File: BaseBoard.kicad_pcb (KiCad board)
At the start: 2 copper layers, 225 x 225 mm, 170 parts, among them Q1 MMBT2222A-7-F, Q10 IRLML6401TRPBF, Q11 MMBT2222A-7-F, Q12 IRLML6401TRPBF, Q13 MMBT2222A-7-F, Q14 IRLML6401TRPBF, Q15 MMBT2222A-7-F, Q16 IRLML6401TRPBF, Q2 IRLML6401TRPBF, Q3 MMBT2222A-7-F, Q4 IRLML6401TRPBF, Q5 MMBT2222A-7-F, Q6 IRLML6401TRPBF, Q7 MMBT2222A-7-F, Q8 IRLML6401TRPBF, Q9 MMBT2222A-7-F, U1 TLC5971PWPR, U10 TLC5971PWPR, U11 TLC5971PWPR, U12 TLC5971PWPR, U13 TLC5971PWPR, U14 TLC5971PWPR, U15 TLC5971PWPR, U16 TLC5971PWPR, U2 TLC5971PWPR, U3 TLC5971PWPR, U4 TLC5971PWPR, U5 TLC5971PWPR, U6 TLC5971PWPR, U7 TLC5971PWPR, U8 TLC5971PWPR, U9 TLC5971PWPR

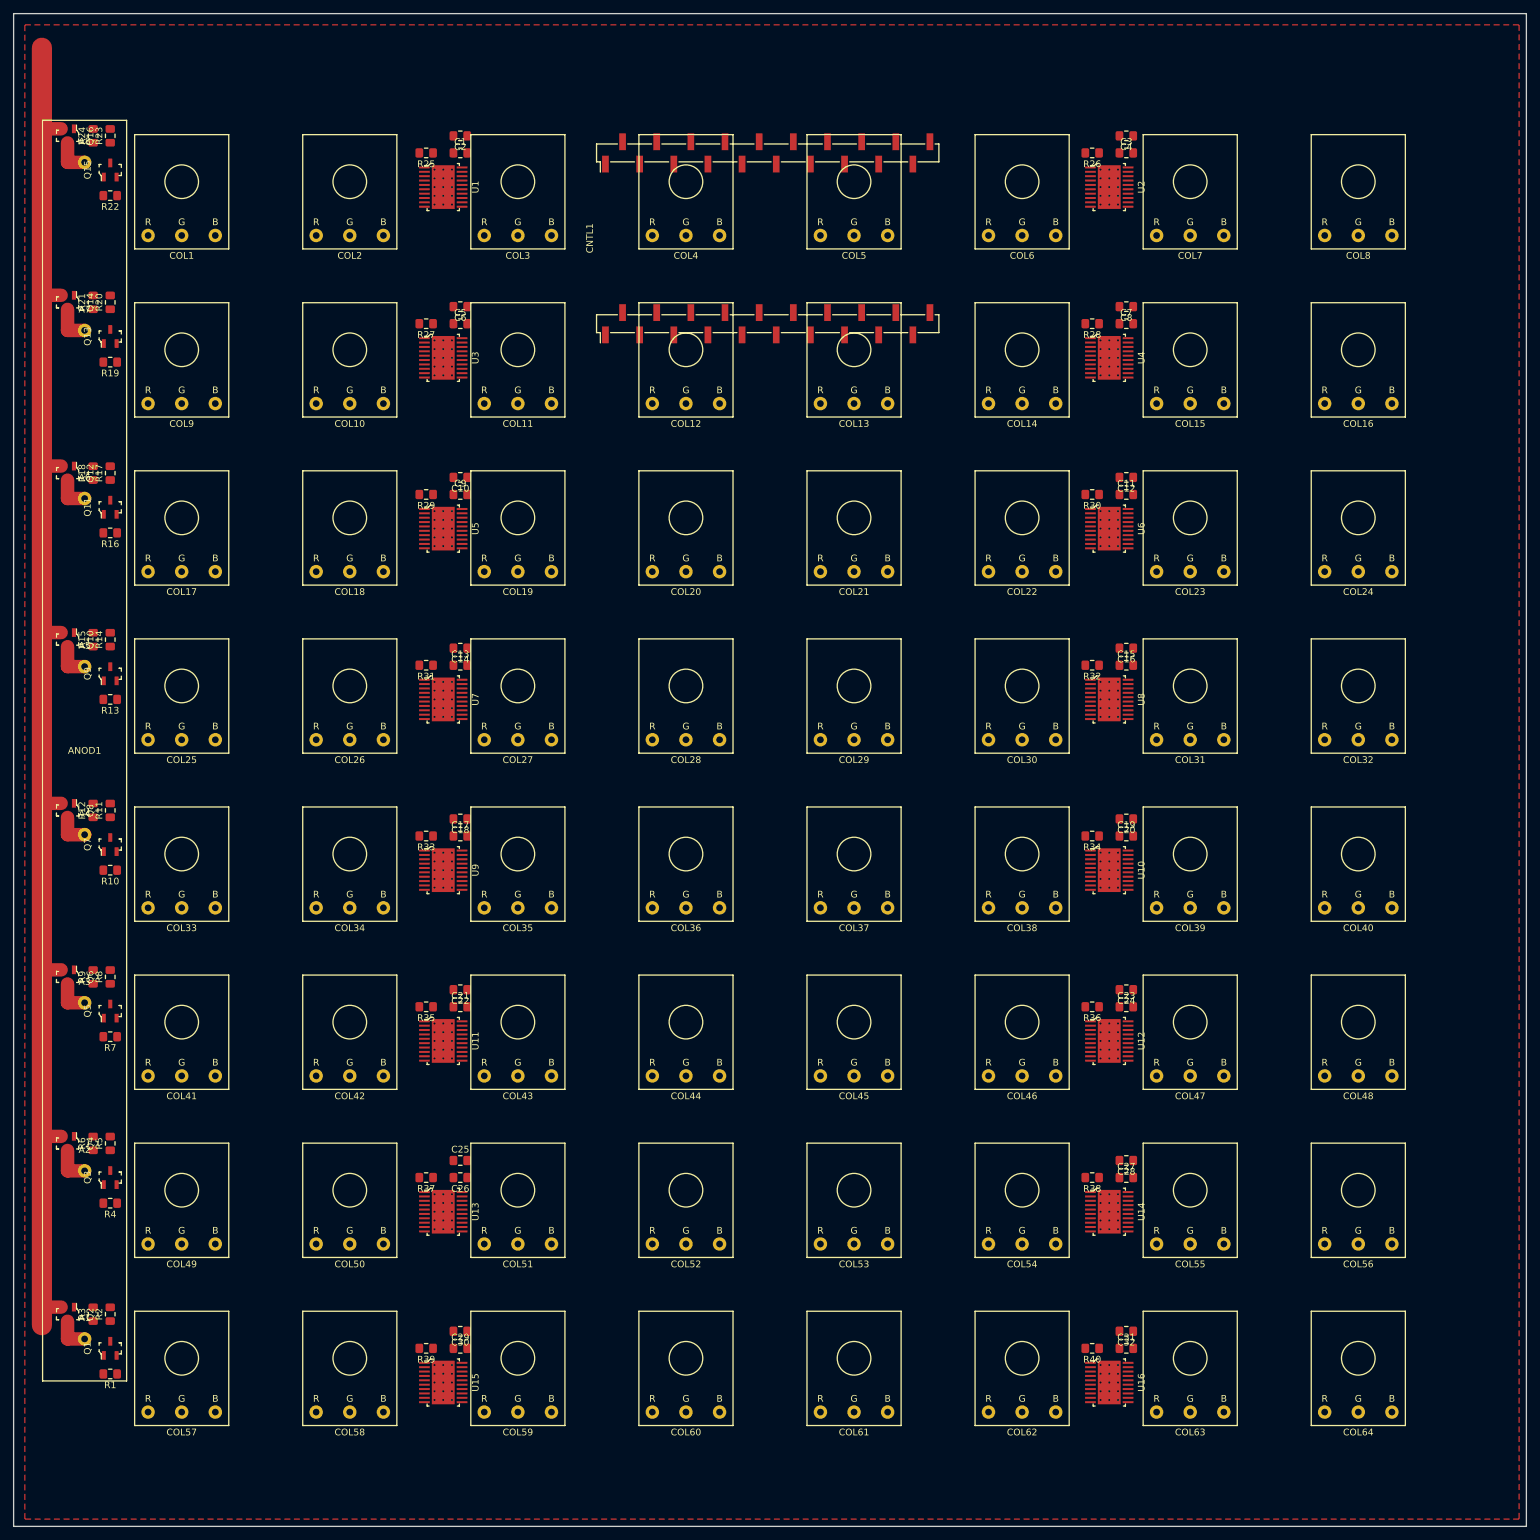
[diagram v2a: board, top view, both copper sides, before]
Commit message: Update footprints
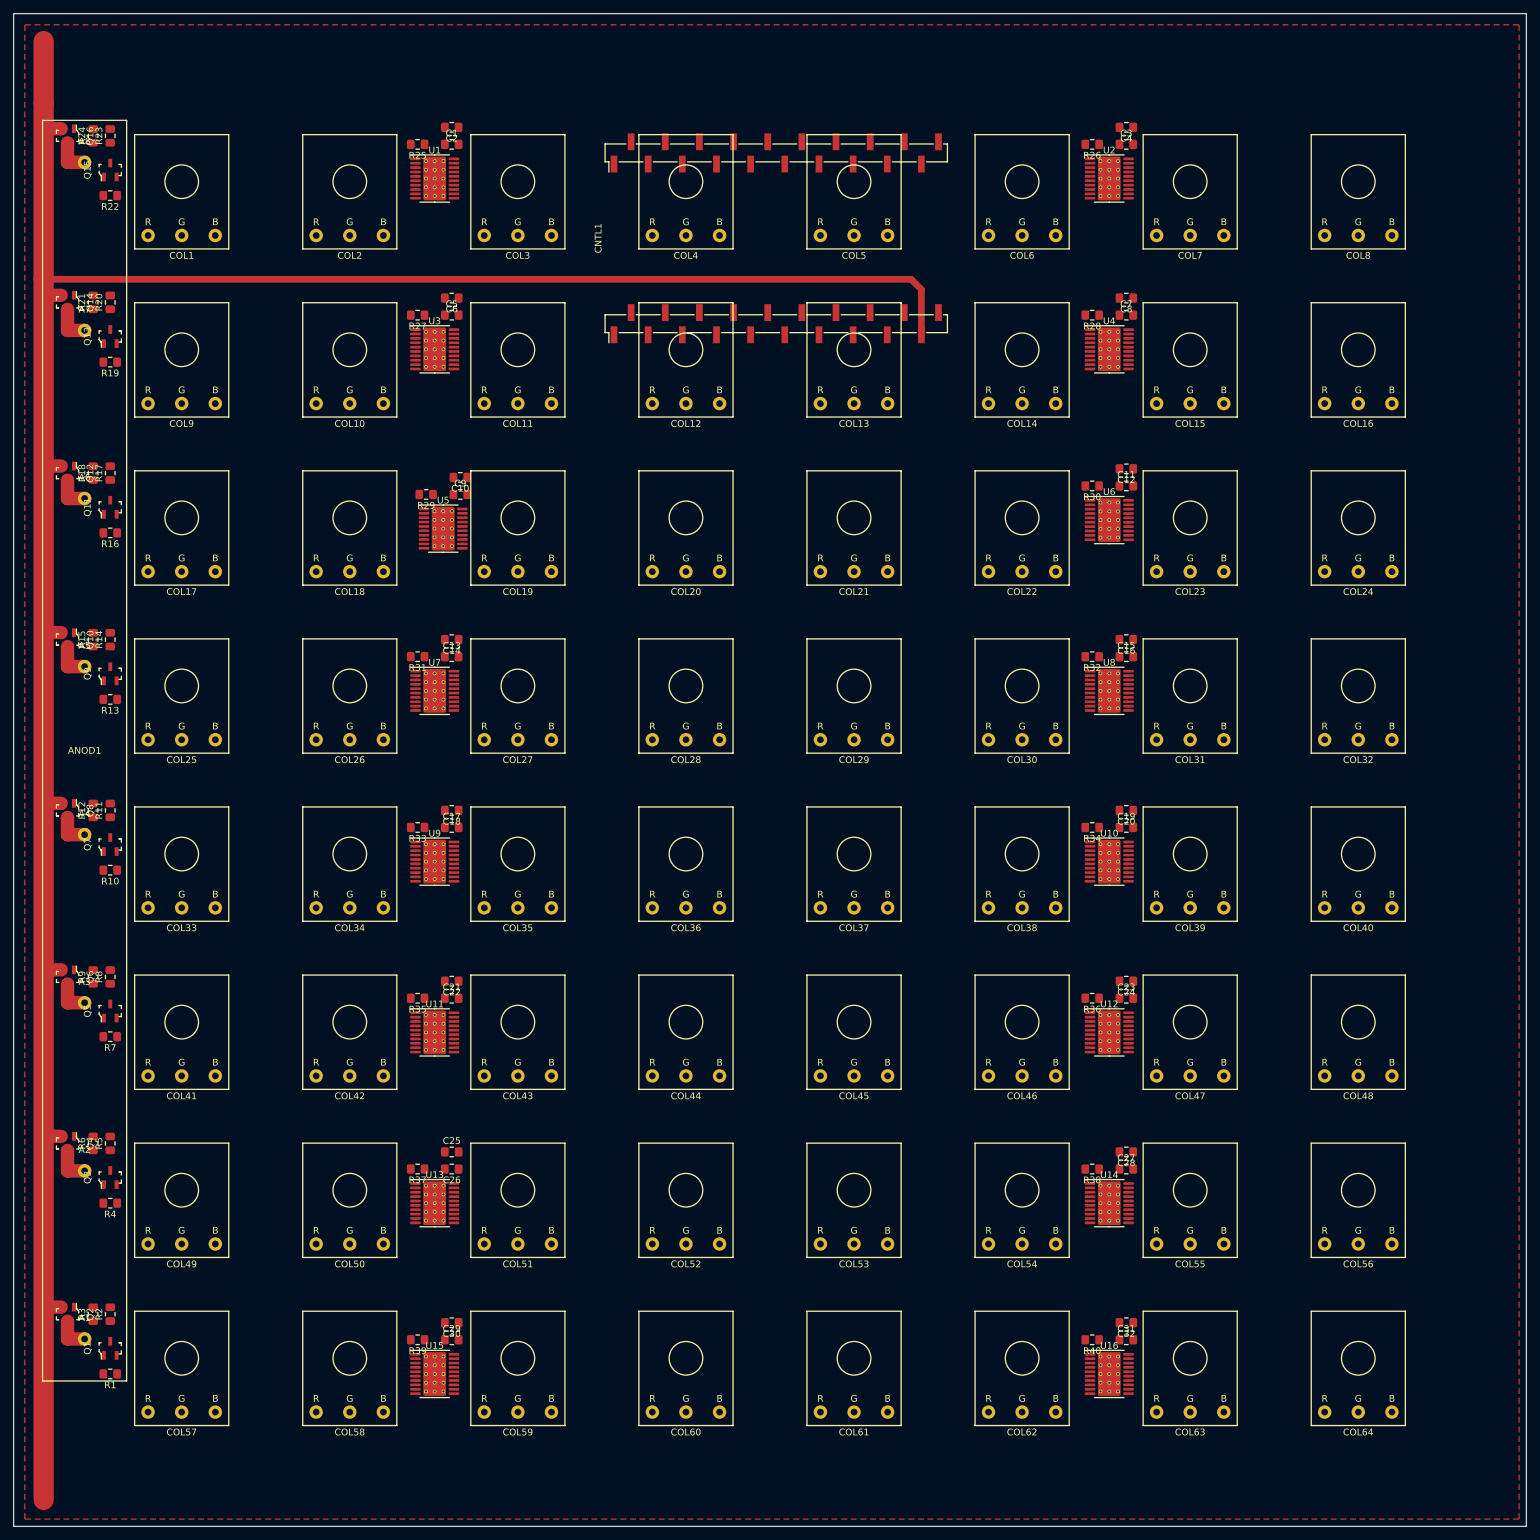
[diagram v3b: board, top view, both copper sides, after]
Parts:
- U1, U10, U11, U12, U13, U14, U15, U16, U2, U3, U4, U5, U6, U7, U8, U9: footprint digikey-footprints:TSSOP-20-1EP_W4.4mm -> Package_SO:HTSSOP-20-1EP_4.4x6.5mm_P0.65mm_EP3.4x6.5mm_Mask2.75x3.43mm_ThermalVias
- moved C13 1.80 mm to (85.1, 115.6)
- moved C17 1.80 mm to (85.1, 141.0)
- moved C25 1.80 mm to (85.1, 189.2)
- moved C29 1.80 mm to (85.1, 217.2)
- moved C30 1.80 mm to (85.1, 214.6)
- moved C5 1.80 mm to (85.1, 64.8)
- moved R27 1.80 mm to (80.0, 64.8)
- moved R31 1.80 mm to (80.0, 115.6)
- moved R33 1.80 mm to (80.0, 141.0)
- moved R39 1.80 mm to (80.0, 217.2)
- moved U11 1.80 mm to (82.5, 171.4), turned to 0 degrees
- moved U13 1.80 mm to (82.5, 196.8), turned to 0 degrees
- moved U15 1.80 mm to (82.5, 222.2), turned to 0 degrees
- moved U3 1.80 mm to (82.5, 69.8), turned to 0 degrees
- moved C1 1.80 mm to (85.1, 39.4)
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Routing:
- net VCC: track 211.3 -> 375.7 mm

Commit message: Improve schematics and PCB
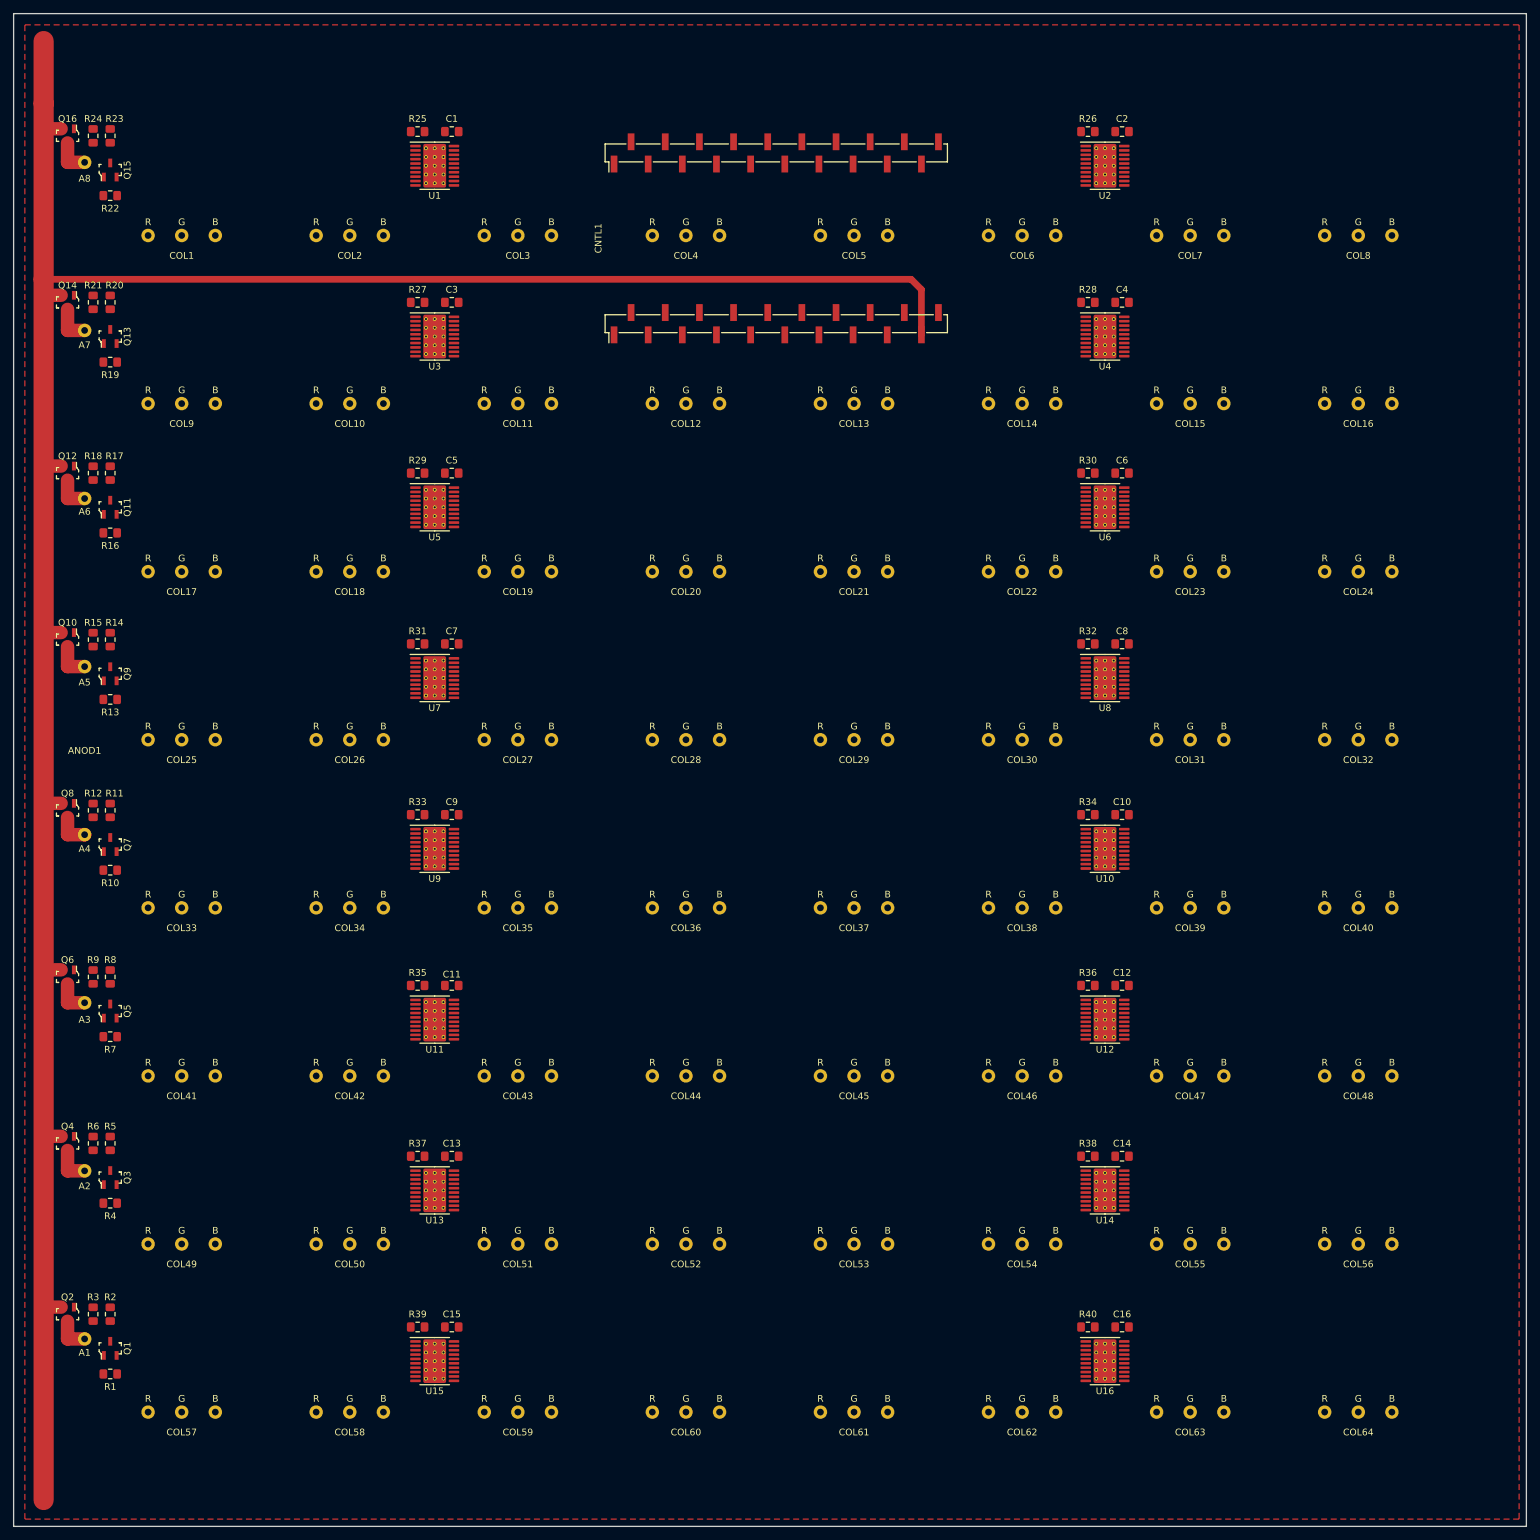
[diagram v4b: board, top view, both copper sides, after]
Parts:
- removed the C10 at (86.4, 88.9)
- removed the C12 at (185.4, 87.6)
- removed the C14 at (85.1, 113.0)
- removed the C16 at (185.4, 113.0)
- removed C17, C18, C20, C21, C22, C24, C25, C26, C28, C29, C30, C32: 1uF, Capacitor_SMD:C_0805_2012Metric_Pad1.15x1.40mm_HandSolder
- removed the C2 at (85.1, 36.8)
- removed the C4 at (185.4, 36.8)
- removed the C6 at (85.1, 62.2)
- removed the C8 at (185.4, 62.2)
- added C11: 1uF, Capacitor_SMD:C_0805_2012Metric_Pad1.15x1.40mm_HandSolder, F.Cu at (85.1, 164.5)
- added C15: 1uF, Capacitor_SMD:C_0805_2012Metric_Pad1.15x1.40mm_HandSolder, F.Cu at (85.1, 215.3)
- added C3: 1uF, Capacitor_SMD:C_0805_2012Metric_Pad1.15x1.40mm_HandSolder, F.Cu at (85.1, 62.9)
- added C7: 1uF, Capacitor_SMD:C_0805_2012Metric_Pad1.15x1.40mm_HandSolder, F.Cu at (85.1, 113.7)
- moved C13 74.3 mm to (85.1, 189.9)
- moved C9 47.6 mm to (85.1, 139.1)
- moved C5 23.5 mm to (85.1, 88.3)
- moved R29 3.42 mm to (80.0, 88.3)
- moved U5 3.42 mm to (82.5, 93.3)
- moved C10 2.01 mm to (184.8, 139.1)
- moved C12 2.01 mm to (184.8, 164.5)
- moved C14 2.01 mm to (184.8, 189.9)
- moved C16 2.01 mm to (184.8, 215.3)
- moved C6 2.01 mm to (184.8, 88.3)
- moved R30 2.01 mm to (179.7, 88.3)
- moved R34 2.01 mm to (179.7, 139.1)
- moved R36 2.01 mm to (179.7, 164.5)
- moved R38 2.01 mm to (179.7, 189.9)
- moved R40 2.01 mm to (179.7, 215.3)
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- renumbered C19 to C10, C23 to C12, C27 to C14, C31 to C16, C3 to C2, C7 to C4, C11 to C6, C15 to C8
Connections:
- U1 pad 20: Net-(C2-Pad1) -> VCC
- U10 pad 20: Net-(C20-Pad1) -> VCC
- U11 pad 20: Net-(C22-Pad1) -> VCC
- U12 pad 20: Net-(C24-Pad1) -> VCC
- U13 pad 20: Net-(C26-Pad1) -> VCC
- U14 pad 20: Net-(C28-Pad1) -> VCC
- U15 pad 20: Net-(C30-Pad1) -> VCC
- U16 pad 20: Net-(C32-Pad1) -> VCC
- U2 pad 20: Net-(C4-Pad1) -> VCC
- U3 pad 20: Net-(C6-Pad1) -> VCC
- U4 pad 20: Net-(C8-Pad1) -> VCC
- U5 pad 20: Net-(C10-Pad1) -> VCC
- U6 pad 20: Net-(C12-Pad1) -> VCC
- U7 pad 20: Net-(C14-Pad1) -> VCC
- U8 pad 20: Net-(C16-Pad1) -> VCC
- U9 pad 20: Net-(C18-Pad1) -> VCC
